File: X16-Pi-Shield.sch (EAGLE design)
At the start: 37 parts, among them J1 CONN_DF13-4P-1.25DSA, J3 CONN_DF13-4P-1.25DSA, J4 HTST-110-04-L-D-RA, J5 BM04B-GHS-TBT, J6 BM04B-GHS-TBT, U1 INA260AIPW, U2 AZ1117IH-3.3TRG1

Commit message: push
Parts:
- added 5V1: (no value), SparkFun-LED:LED0603
- added JP1: (no value), X16-ExtraComponents:TEST_PIN-1X3
- added R1: 150, SparkFun-Resistors:RESISTOR0603
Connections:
- new net LEAK: JP1.1, U$1.GPIO12
- new net N$3: U$2.3VO
- new net N$4: U$3.3VO
- new net N$5: U$3.3VO
- new net N$6: 5V1.A, R1.1
- net 3V3: now also JP1.2
- net 5V_EXT: now also R1.2
- net GND: now also 5V1.C, JP1.3
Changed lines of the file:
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@@
 <part name="J6" library="X16-Pi-Shield" deviceset="BM04B-GHS-TBT" device=""/>
 <part name="GND23" library="supply1" library_urn="urn:adsk.eagle:library:371" deviceset="GND" device=""/>
+<part name="JP1" library="X16-ExtraComponents" deviceset="TEST_PIN-1X3" device="" package3d_urn="urn:adsk.eagle:package:22458/2"/>
+<part name="5V1" library="SparkFun-LED" deviceset="LED" device="0603"/>
+<part name="R1" library="SparkFun-Resistors" deviceset="RESISTOR" device="0603" value="150"/>
+<part name="GND24" library="SparkFun-PowerSymbols" library_urn="urn:adsk.eagle:library:530" deviceset="GND" device=""/>
 </parts>
 <sheets>
@@
 </segment>
 </net>
+<net name="N$3" class="0">
+<segment>
+<pinref part="U$2" gate="G$1" pin="3VO"/>
+<wire x1="76.2" y1="104.14" x2="83.82" y2="104.14" width="0.1524" layer="91"/>
+</segment>
+</net>
+<net name="N$4" class="0">
+<segment>
+<pinref part="U$3" gate="G$1" pin="3VO"/>
+<wire x1="147.32" y1="91.44" x2="137.16" y2="91.44" width="0.1524" layer="91"/>
+</segment>
+</net>
+<net name="LEAK" class="0">
+<segment>
+<pinref part="U$1" gate="G$1" pin="GPIO12"/>
+<wire x1="190.5" y1="160.02" x2="190.5" y2="167.64" width="0.1524" layer="91"/>
+<label x="190.5" y="162.56" size="1.778" layer="95" rot="R90"/>
+</segment>
+</net>
 </nets>
 </sheet>
@@
 <attribute name="VALUE" x="93.98" y="70.866" size="1.778" layer="96" align="top-center"/>
 </instance>
+<instance part="5V1" gate="G$1" x="144.78" y="71.12" smashed="yes">
+<attribute name="NAME" x="141.351" y="66.548" size="1.778" layer="95" font="vector" rot="R90"/>
+<attribute name="VALUE" x="146.685" y="66.548" size="1.778" layer="96" font="vector" rot="R90" align="top-left"/>
+</instance>
+<instance part="R1" gate="G$1" x="144.78" y="88.9" smashed="yes" rot="R90">
+<attribute name="NAME" x="143.256" y="88.9" size="1.778" layer="95" font="vector" rot="R90" align="bottom-center"/>
+<attribute name="VALUE" x="146.304" y="88.9" size="1.778" layer="96" font="vector" rot="R90" align="top-center"/>
+</instance>
+<instance part="GND24" gate="1" x="144.78" y="60.96" smashed="yes">
+<attribute name="VALUE" x="144.78" y="60.706" size="1.778" layer="96" align="top-center"/>
+</instance>
 </instances>
 <busses>
@@
 <pinref part="GND22" gate="1" pin="GND"/>
 </segment>
+<segment>
+<pinref part="5V1" gate="G$1" pin="C"/>
+<wire x1="144.78" y1="66.04" x2="144.78" y2="63.5" width="0.1524" layer="91"/>
+<pinref part="GND24" gate="1" pin="GND"/>
+</segment>
 </net>
 <net name="3V3" class="0">
@@
 <wire x1="93.98" y1="78.74" x2="93.98" y2="81.28" width="0.1524" layer="91"/>
 <label x="91.44" y="81.28" size="1.778" layer="95"/>
+</segment>
+<segment>
+<pinref part="R1" gate="G$1" pin="2"/>
+<wire x1="144.78" y1="93.98" x2="144.78" y2="99.06" width="0.1524" layer="91"/>
+<label x="144.78" y="99.06" size="1.778" layer="95"/>
 </segment>
 </net>
@@
 </segment>
 </net>
+<net name="N$6" class="0">
+<segment>
+<pinref part="R1" gate="G$1" pin="1"/>
+<pinref part="5V1" gate="G$1" pin="A"/>
+<wire x1="144.78" y1="83.82" x2="144.78" y2="73.66" width="0.1524" layer="91"/>
+</segment>
+</net>
 </nets>
 </sheet>
@@
 <attribute name="VALUE" x="121.92" y="60.706" size="1.778" layer="96" align="top-center"/>
 </instance>
+<instance part="JP1" gate="A" x="40.64" y="127" smashed="yes">
+<attribute name="NAME" x="34.29" y="132.715" size="1.778" layer="95"/>
+<attribute name="VALUE" x="34.29" y="119.38" size="1.778" layer="96"/>
+</instance>
 </instances>
 <busses>
@@
 <pinref part="GND21" gate="1" pin="GND"/>
 </segment>
+<segment>
+<pinref part="JP1" gate="A" pin="3"/>
+<wire x1="35.56" y1="124.46" x2="27.94" y2="124.46" width="0.1524" layer="91"/>
+<label x="27.94" y="124.46" size="1.778" layer="95"/>
+</segment>
 </net>
 <net name="3V3" class="0">
@@
 <label x="120.65" y="105.41" size="1.778" layer="95" rot="R90"/>
 </segment>
+<segment>
+<pinref part="JP1" gate="A" pin="2"/>
+<wire x1="35.56" y1="127" x2="27.94" y2="127" width="0.1524" layer="91"/>
+<label x="27.94" y="127" size="1.778" layer="95"/>
+</segment>
 </net>
 <net name="IMU_INT_2" class="0">
@@
 </segment>
 </net>
+<net name="N$5" class="0">
+<segment>
+<pinref part="U$3" gate="G$1" pin="3VO"/>
+<wire x1="137.16" y1="91.44" x2="144.78" y2="91.44" width="0.1524" layer="91"/>
+<wire x1="149.86" y1="91.44" x2="144.78" y2="91.44" width="0.1524" layer="91"/>
+</segment>
+</net>
+<net name="LEAK" class="0">
+<segment>
+<pinref part="JP1" gate="A" pin="1"/>
+<wire x1="35.56" y1="129.54" x2="27.94" y2="129.54" width="0.1524" layer="91"/>
+<label x="27.94" y="129.54" size="1.778" layer="95"/>
+</segment>
+</net>

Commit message: Minh Update
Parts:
- C1, C2: value 120uF -> 10uF
- C4: value 10uF -> 2.2uF
- C5: value 22uF -> 2.2uF
- R1, R15: value 150 -> (none)
- R11, R12: value 10k -> (none)
- R16: value 60 -> (none)
- renumbered 5V1 to 5V_EXT
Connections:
- removed net N$4: U$3.3VO

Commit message: Minh Update 2
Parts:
- 3V, 5V, 5V_EXT: device SparkFun-LED:LED0603 -> led:LEDCHIPLED_0805
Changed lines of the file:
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@@
 <part name="GND29" library="SparkFun-PowerSymbols" library_urn="urn:adsk.eagle:library:530" deviceset="GND" device=""/>
 <part name="FRAME2" library="SparkFun-Aesthetics" deviceset="FRAME-A4L" device=""/>
-<part name="5V" library="SparkFun-LED" library_urn="urn:adsk.eagle:library:529" deviceset="LED" device="0603" package3d_urn="urn:adsk.eagle:package:39354/1"/>
-<part name="3V" library="SparkFun-LED" library_urn="urn:adsk.eagle:library:529" deviceset="LED" device="0603" package3d_urn="urn:adsk.eagle:package:39354/1"/>
+<part name="5V" library="led" library_urn="urn:adsk.eagle:library:259" deviceset="LED" device="CHIPLED_0805" package3d_urn="urn:adsk.eagle:package:15821/2"/>
+<part name="3V" library="led" library_urn="urn:adsk.eagle:library:259" deviceset="LED" device="CHIPLED_0805" package3d_urn="urn:adsk.eagle:package:15821/2"/>
 <part name="R15" library="SparkFun-Resistors" library_urn="urn:adsk.eagle:library:532" deviceset="RESISTOR" device="0603" package3d_urn="urn:adsk.eagle:package:39650/1" value=" "/>
 <part name="R16" library="SparkFun-Resistors" library_urn="urn:adsk.eagle:library:532" deviceset="RESISTOR" device="0603" package3d_urn="urn:adsk.eagle:package:39650/1" value=" "/>
@@
 <part name="GND23" library="supply1" library_urn="urn:adsk.eagle:library:371" deviceset="GND" device=""/>
 <part name="JP1" library="X16-ExtraComponents" deviceset="TEST_PIN-1X3" device="" package3d_urn="urn:adsk.eagle:package:22458/2"/>
-<part name="5V_EXT" library="SparkFun-LED" library_urn="urn:adsk.eagle:library:529" deviceset="LED" device="0603" package3d_urn="urn:adsk.eagle:package:39354/1"/>
+<part name="5V_EXT" library="led" library_urn="urn:adsk.eagle:library:259" deviceset="LED" device="CHIPLED_0805" package3d_urn="urn:adsk.eagle:package:15821/2"/>
 <part name="R1" library="SparkFun-Resistors" library_urn="urn:adsk.eagle:library:532" deviceset="RESISTOR" device="0603" package3d_urn="urn:adsk.eagle:package:39650/1" value=" "/>
 <part name="GND24" library="SparkFun-PowerSymbols" library_urn="urn:adsk.eagle:library:530" deviceset="GND" device=""/>

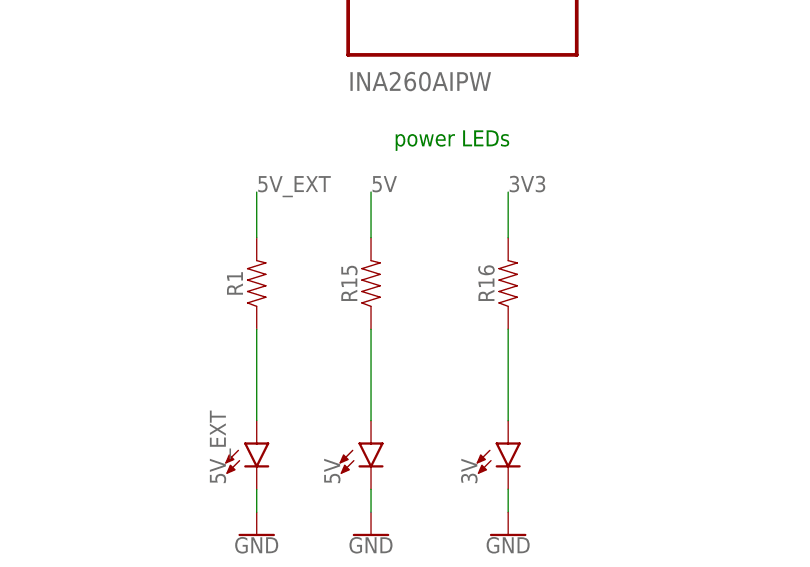
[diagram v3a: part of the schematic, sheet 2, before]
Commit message: Added resistor values. Make sure to update BOM!
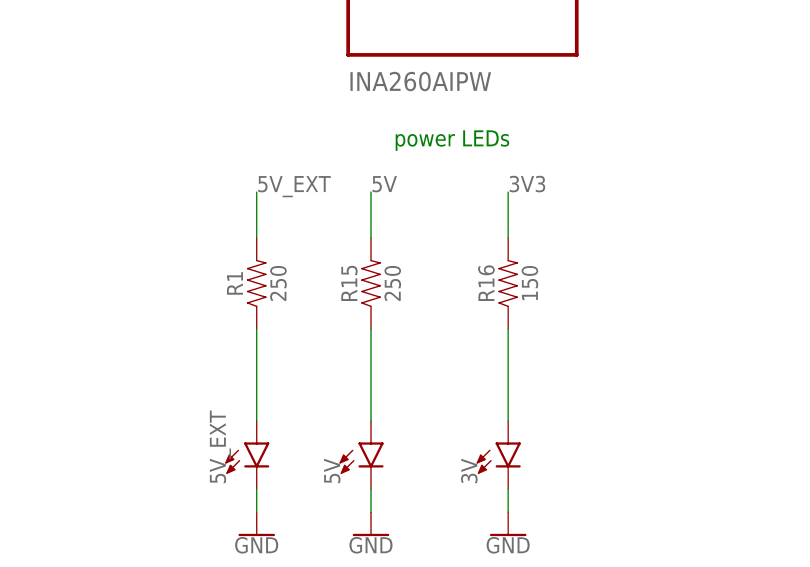
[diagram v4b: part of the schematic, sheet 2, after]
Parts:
- R1, R15: value (none) -> 250
- R11, R12: value (none) -> 10k
- R16: value (none) -> 150
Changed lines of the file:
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@@
 <part name="J7" library="SparkFun-Connectors" library_urn="urn:adsk.eagle:library:513" deviceset="CONN_03" device="" package3d_urn="urn:adsk.eagle:package:38063/1"/>
 <part name="GND28" library="SparkFun-PowerSymbols" library_urn="urn:adsk.eagle:library:530" deviceset="GND" device=""/>
-<part name="R11" library="SparkFun-Resistors" library_urn="urn:adsk.eagle:library:532" deviceset="RESISTOR" device="0603" package3d_urn="urn:adsk.eagle:package:39650/1" value=" "/>
-<part name="R12" library="SparkFun-Resistors" library_urn="urn:adsk.eagle:library:532" deviceset="RESISTOR" device="0603" package3d_urn="urn:adsk.eagle:package:39650/1" value=" "/>
+<part name="R11" library="SparkFun-Resistors" library_urn="urn:adsk.eagle:library:532" deviceset="RESISTOR" device="0603" package3d_urn="urn:adsk.eagle:package:39650/1" value="10k"/>
+<part name="R12" library="SparkFun-Resistors" library_urn="urn:adsk.eagle:library:532" deviceset="RESISTOR" device="0603" package3d_urn="urn:adsk.eagle:package:39650/1" value="10k"/>
 <part name="J11" library="SparkFun-Connectors" library_urn="urn:adsk.eagle:library:513" deviceset="CONN_04" device="" package3d_urn="urn:adsk.eagle:package:38085/1"/>
 <part name="GND29" library="SparkFun-PowerSymbols" library_urn="urn:adsk.eagle:library:530" deviceset="GND" device=""/>
@@
 <part name="5V" library="led" library_urn="urn:adsk.eagle:library:259" deviceset="LED" device="CHIPLED_0805" package3d_urn="urn:adsk.eagle:package:15821/2"/>
 <part name="3V" library="led" library_urn="urn:adsk.eagle:library:259" deviceset="LED" device="CHIPLED_0805" package3d_urn="urn:adsk.eagle:package:15821/2"/>
-<part name="R15" library="SparkFun-Resistors" library_urn="urn:adsk.eagle:library:532" deviceset="RESISTOR" device="0603" package3d_urn="urn:adsk.eagle:package:39650/1" value=" "/>
-<part name="R16" library="SparkFun-Resistors" library_urn="urn:adsk.eagle:library:532" deviceset="RESISTOR" device="0603" package3d_urn="urn:adsk.eagle:package:39650/1" value=" "/>
+<part name="R15" library="SparkFun-Resistors" library_urn="urn:adsk.eagle:library:532" deviceset="RESISTOR" device="0603" package3d_urn="urn:adsk.eagle:package:39650/1" value="250"/>
+<part name="R16" library="SparkFun-Resistors" library_urn="urn:adsk.eagle:library:532" deviceset="RESISTOR" device="0603" package3d_urn="urn:adsk.eagle:package:39650/1" value="150"/>
 <part name="GND43" library="SparkFun-PowerSymbols" library_urn="urn:adsk.eagle:library:530" deviceset="GND" device=""/>
 <part name="GND44" library="SparkFun-PowerSymbols" library_urn="urn:adsk.eagle:library:530" deviceset="GND" device=""/>
@@
 <part name="JP1" library="X16-ExtraComponents" deviceset="TEST_PIN-1X3" device="" package3d_urn="urn:adsk.eagle:package:22458/2"/>
 <part name="5V_EXT" library="led" library_urn="urn:adsk.eagle:library:259" deviceset="LED" device="CHIPLED_0805" package3d_urn="urn:adsk.eagle:package:15821/2"/>
-<part name="R1" library="SparkFun-Resistors" library_urn="urn:adsk.eagle:library:532" deviceset="RESISTOR" device="0603" package3d_urn="urn:adsk.eagle:package:39650/1" value=" "/>
+<part name="R1" library="SparkFun-Resistors" library_urn="urn:adsk.eagle:library:532" deviceset="RESISTOR" device="0603" package3d_urn="urn:adsk.eagle:package:39650/1" value="250"/>
 <part name="GND24" library="SparkFun-PowerSymbols" library_urn="urn:adsk.eagle:library:530" deviceset="GND" device=""/>
 </parts>
